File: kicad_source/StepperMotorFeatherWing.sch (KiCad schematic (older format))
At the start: 14 parts, among them CN1 ADAFRUIT_FEATHER, P10 CONN_01X04, P7 CONN_01X04, P8 CONN_01X04, P9 CONN_01X04, Y1 oscillator

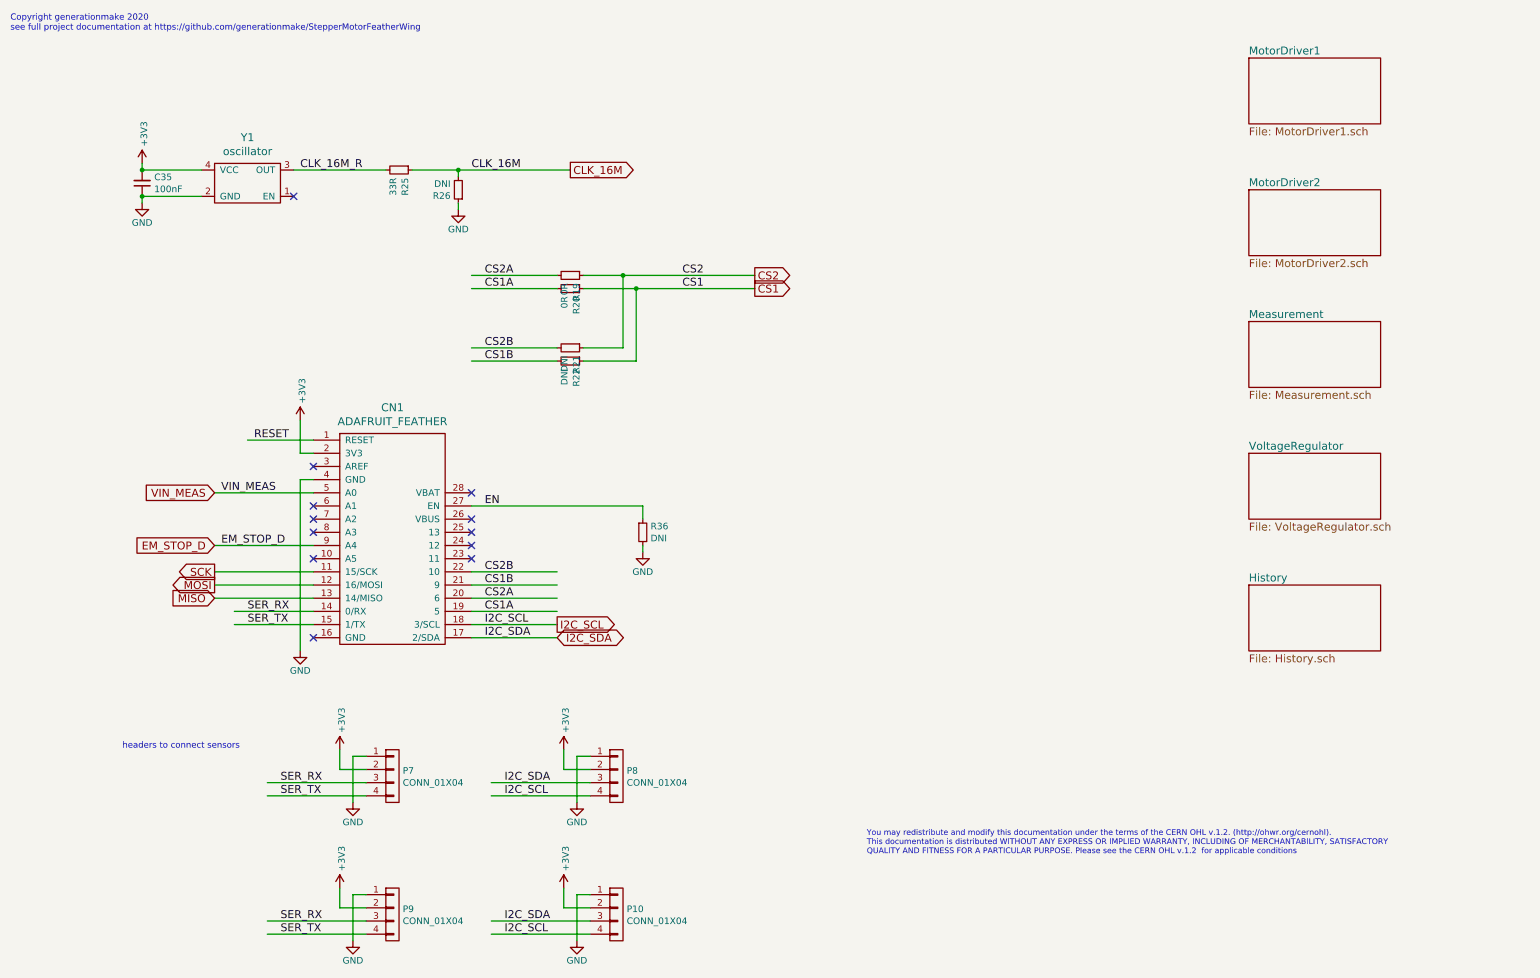
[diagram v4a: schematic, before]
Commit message: added expansion connector, updated layout
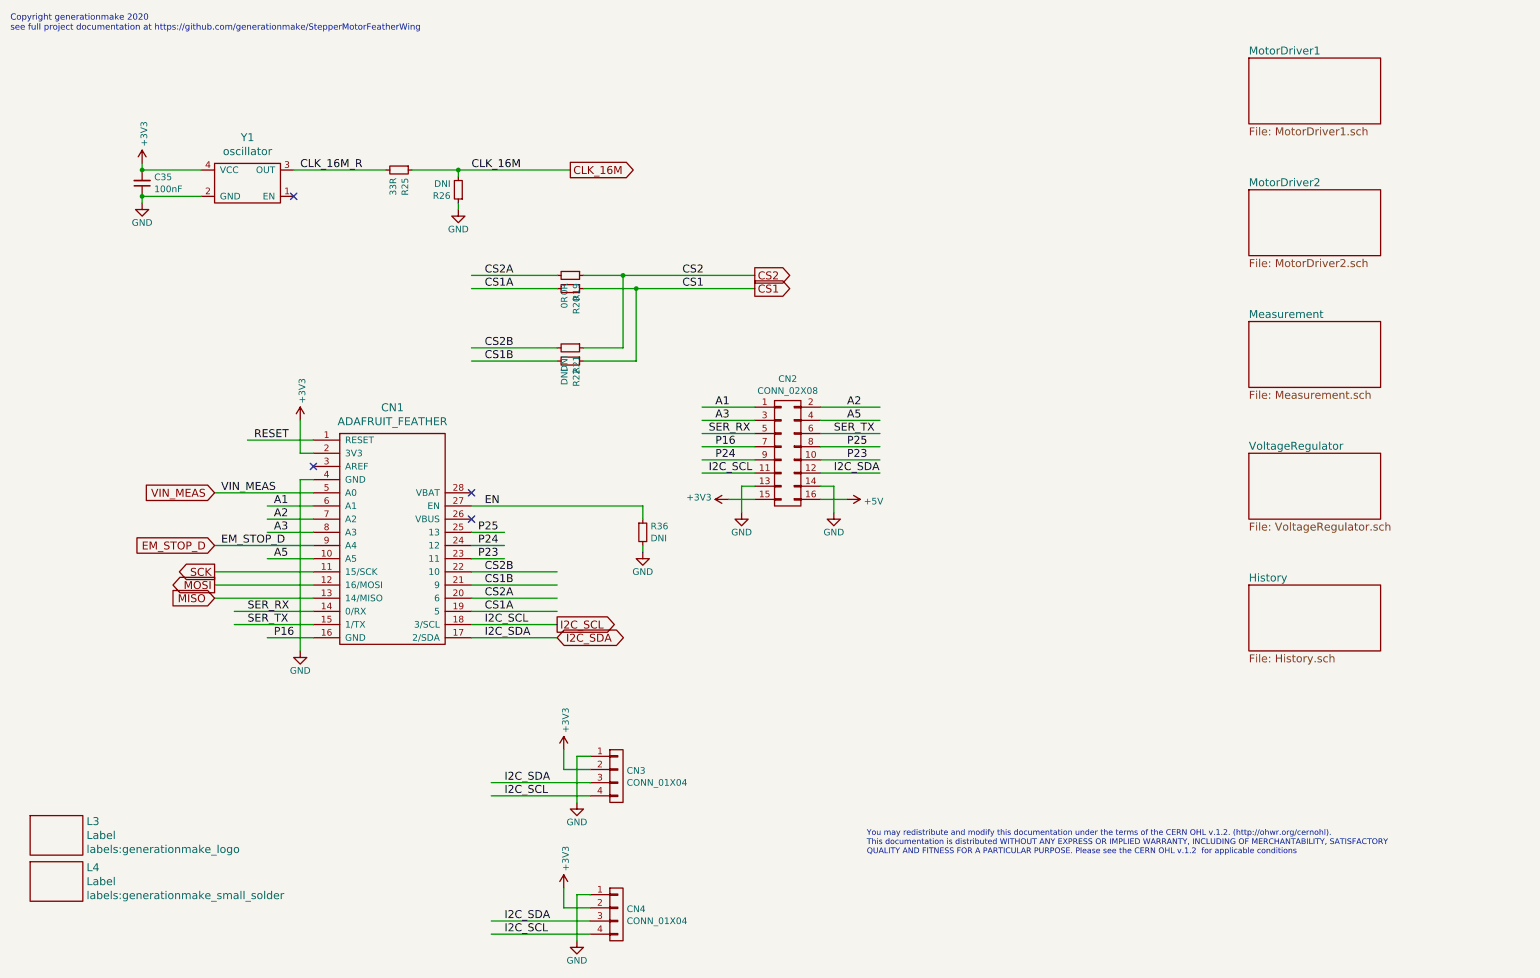
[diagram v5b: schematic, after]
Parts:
- removed P7: CONN_01X04, connectors_JST_SH:Connectors_JST_BM04B-SRSS-TB, symbol mechanical-connectors:CONN_01X04
- removed P9: CONN_01X04, pin_headers:Pin_Header_Straight_1x04, symbol mechanical-connectors:CONN_01X04
- added CN2: CONN_02X08, pin_headers:Pin_Header_Straight_2x08, symbol mechanical-connectors:CONN_02X08
- added L3: Label, labels:generationmake_logo, symbol devices:Label
- added L4: Label, labels:generationmake_small_solder, symbol devices:Label
- renumbered P8 to CN3, P10 to CN4
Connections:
- net labels added: +5V, A1, A2, A3, A5, P16, P23, P24, P25
- wire segments 66 -> 80
- no-connect marks 12 -> 4
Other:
- note removed: "headers to connect sensors"
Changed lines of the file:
@@
 Sheet 1 6
 Title "HighPowerMotorFeatherWing"
-Date "2020-07-04"
+Date "2020-07-08"
 Rev "1.1"
 Comp "generationmake"
@@
 	2050 4150 2800 4150
 NoConn ~ 2800 3950
-NoConn ~ 2800 4250
-NoConn ~ 2800 4350
-NoConn ~ 2800 4450
-NoConn ~ 2800 4650
 NoConn ~ 4000 4350
 NoConn ~ 4000 4150
@@
 Wire Wire Line
 	2700 4050 2700 5350
-NoConn ~ 2800 5250
 $Sheet
 S 9900 3850 1000 500
@@
 Wire Wire Line
 	2050 4550 2800 4550
-NoConn ~ 4000 4450
 $Comp
 L devices:R_0603 R36
@@
 Text GLabel 2050 4950 0    60   Input ~ 0
 MISO
-NoConn ~ 4000 4650
-NoConn ~ 4000 4550
 Text GLabel 6150 2500 2    60   Output ~ 0
 CS2
@@
 CS2
 $Comp
-L mechanical-connectors:CONN_01X04 P8
+L mechanical-connectors:CONN_01X04 CN3
 U 1 1 5DFC9702
 P 5100 6300
-F 0 "P8" H 5178 6341 50  0000 L CNN
+F 0 "CN3" H 5178 6341 50  0000 L CNN
 F 1 "CONN_01X04" H 5178 6250 50  0000 L CNN
 F 2 "connectors_JST_SH:Connectors_JST_BM04B-SRSS-TB" H 5100 6300 50  0001 C CNN
@@
 Text Label 4250 6450 0    60   ~ 0
 I2C_SCL
-$Comp
-L mechanical-connectors:CONN_01X04 P7
-U 1 1 5DFCD1B4
-P 3400 6300
-F 0 "P7" H 3478 6341 50  0000 L CNN
-F 1 "CONN_01X04" H 3478 6250 50  0000 L CNN
-F 2 "connectors_JST_SH:Connectors_JST_BM04B-SRSS-TB" H 3478 6204 50  0001 L CNN
-F 3 "" H 3400 6300 50  0000 C CNN
-	1    3400 6300
-	1    0    0    -1
-$EndComp
-$Comp
-L StepperMotorFeatherWing-rescue:+3V3-power-supply-MKRHMIShield-rescue-MKRHMIShield-rescue-HMIFeatherWing-rescue-HighPowerMotorFeatherWing-rescue #PWR078
-U 1 1 5DFCD1BE
-P 3000 6100
-F 0 "#PWR078" H 3000 5950 50  0001 C CNN
-F 1 "+3V3" V 3015 6228 50  0000 L CNN
-F 2 "" H 3000 6100 50  0000 C CNN
-F 3 "" H 3000 6100 50  0000 C CNN
-	1    3000 6100
-	1    0    0    -1
-$EndComp
-$Comp
-L StepperMotorFeatherWing-rescue:GND-ArduHMIShield-rescue-ArduHMIShield-rescue-MKRHMIShield-rescue-MKRHMIShield-rescue-HMIFeatherWing-rescue-HighPowerMotorFeatherWing-rescue #PWR081
-U 1 1 5DFCD1C8
-P 3100 6500
-F 0 "#PWR081" H 3100 6250 50  0001 C CNN
-F 1 "GND" H 3100 6350 50  0000 C CNN
-F 2 "" H 3100 6500 50  0000 C CNN
-F 3 "" H 3100 6500 50  0000 C CNN
-	1    3100 6500
-	1    0    0    -1
-$EndComp
-Wire Wire Line
-	3200 6150 3100 6150
-Wire Wire Line
-	3100 6150 3100 6500
-Wire Wire Line
-	3200 6250 3000 6250
-Wire Wire Line
-	3000 6250 3000 6100
-Wire Wire Line
-	2450 6350 3200 6350
-Wire Wire Line
-	2450 6450 3200 6450
-Text Label 2550 6350 0    60   ~ 0
-SER_RX
-Text Label 2550 6450 0    60   ~ 0
-SER_TX
 Wire Wire Line
 	2200 5050 2800 5050
@@
 SER_TX
 $Comp
-L mechanical-connectors:CONN_01X04 P10
+L mechanical-connectors:CONN_01X04 CN4
 U 1 1 5DF94AD6
 P 5100 7350
-F 0 "P10" H 5178 7391 50  0000 L CNN
+F 0 "CN4" H 5178 7391 50  0000 L CNN
 F 1 "CONN_01X04" H 5178 7300 50  0000 L CNN
 F 2 "pin_headers:Pin_Header_Straight_1x04" H 5100 7350 50  0001 C CNN
@@
 Text Label 4250 7500 0    60   ~ 0
 I2C_SCL
-$Comp
-L mechanical-connectors:CONN_01X04 P9
-U 1 1 5DF94AFC
-P 3400 7350
-F 0 "P9" H 3478 7391 50  0000 L CNN
-F 1 "CONN_01X04" H 3478 7300 50  0000 L CNN
-F 2 "pin_headers:Pin_Header_Straight_1x04" H 3478 7254 50  0001 L CNN
-F 3 "" H 3400 7350 50  0000 C CNN
-	1    3400 7350
-	1    0    0    -1
-$EndComp
-$Comp
-L StepperMotorFeatherWing-rescue:+3V3-power-supply-MKRHMIShield-rescue-MKRHMIShield-rescue-HMIFeatherWing-rescue-HighPowerMotorFeatherWing-rescue #PWR083
-U 1 1 5DF94B06
-P 3000 7150
-F 0 "#PWR083" H 3000 7000 50  0001 C CNN
-F 1 "+3V3" V 3015 7278 50  0000 L CNN
-F 2 "" H 3000 7150 50  0000 C CNN
-F 3 "" H 3000 7150 50  0000 C CNN
-	1    3000 7150
-	1    0    0    -1
-$EndComp
-$Comp
-L StepperMotorFeatherWing-rescue:GND-ArduHMIShield-rescue-ArduHMIShield-rescue-MKRHMIShield-rescue-MKRHMIShield-rescue-HMIFeatherWing-rescue-HighPowerMotorFeatherWing-rescue #PWR085
-U 1 1 5DF94B10
-P 3100 7550
-F 0 "#PWR085" H 3100 7300 50  0001 C CNN
-F 1 "GND" H 3100 7400 50  0000 C CNN
-F 2 "" H 3100 7550 50  0000 C CNN
-F 3 "" H 3100 7550 50  0000 C CNN
-	1    3100 7550
-	1    0    0    -1
-$EndComp
-Wire Wire Line
-	3200 7200 3100 7200
-Wire Wire Line
-	3100 7200 3100 7550
-Wire Wire Line
-	3200 7300 3000 7300
-Wire Wire Line
-	3000 7300 3000 7150
-Wire Wire Line
-	2450 7400 3200 7400
-Wire Wire Line
-	2450 7500 3200 7500
-Text Label 2550 7400 0    60   ~ 0
-SER_RX
-Text Label 2550 7500 0    60   ~ 0
-SER_TX
-Text Notes 1350 6100 0    47   ~ 0
-headers to connect sensors
 $Comp
 L devices:R_0603 R19
@@
 Text GLabel 4750 1700 2    60   Output ~ 0
 CLK_16M
+$Comp
+L mechanical-connectors:CONN_02X08 CN2
+U 1 1 5F051404
+P 6400 3850
+F 0 "CN2" H 6400 4415 50  0000 C CNN
+F 1 "CONN_02X08" H 6400 4324 50  0000 C CNN
+F 2 "pin_headers:Pin_Header_Straight_2x08" H 6400 2650 50  0001 C CNN
+F 3 "" H 6400 2650 50  0000 C CNN
+	1    6400 3850
+	1    0    0    -1
+$EndComp
+Wire Wire Line
+	2450 4650 2800 4650
+Wire Wire Line
+	2450 4450 2800 4450
+Wire Wire Line
+	2450 4350 2800 4350
+Wire Wire Line
+	2450 4250 2800 4250
+Text Label 2500 4250 0    60   ~ 0
+A1
+Text Label 2500 4350 0    60   ~ 0
+A2
+Text Label 2500 4450 0    60   ~ 0
+A3
+Text Label 2500 4650 0    60   ~ 0
+A5
+Wire Wire Line
+	2450 5250 2800 5250
+Text Label 2500 5250 0    60   ~ 0
+P16
+Wire Wire Line
+	4250 4650 4000 4650
+Wire Wire Line
+	4250 4550 4000 4550
+Wire Wire Line
+	4250 4450 4000 4450
+Text Label 4050 4650 0    60   ~ 0
+P23
+Text Label 4050 4550 0    60   ~ 0
+P24
+Text Label 4050 4450 0    60   ~ 0
+P25
+Wire Wire Line
+	5750 3500 6150 3500
+Wire Wire Line
+	5750 3600 6150 3600
+Wire Wire Line
+	5750 3700 6150 3700
+Wire Wire Line
+	5750 3800 6150 3800
+Wire Wire Line
+	5750 3900 6150 3900
+Wire Wire Line
+	6650 3900 7100 3900
+Wire Wire Line
+	7100 3800 6650 3800
+Wire Wire Line
+	6650 3700 7100 3700
+Wire Wire Line
+	7100 3600 6650 3600
+Wire Wire Line
+	7100 3500 6650 3500
+Text Label 5850 3500 0    60   ~ 0
+A1
+Text Label 6850 3500 0    60   ~ 0
+A2
+Text Label 5850 3600 0    60   ~ 0
+A3
+Text Label 6850 3600 0    60   ~ 0
+A5
+Text Label 5800 3700 0    60   ~ 0
+SER_RX
+Text Label 6750 3700 0    60   ~ 0
+SER_TX
+Text Label 5850 3800 0    60   ~ 0
+P16
+Text Label 6850 3800 0    60   ~ 0
+P25
+Text Label 5850 3900 0    60   ~ 0
+P24
+Text Label 6850 3900 0    60   ~ 0
+P23
+$Comp
+L StepperMotorFeatherWing-rescue:GND-ArduHMIShield-rescue-ArduHMIShield-rescue-MKRHMIShield-rescue-MKRHMIShield-rescue-HMIFeatherWing-rescue-HighPowerMotorFeatherWing-rescue #PWR081
+U 1 1 5F086557
+P 6050 4300
+F 0 "#PWR081" H 6050 4050 50  0001 C CNN
+F 1 "GND" H 6050 4150 50  0000 C CNN
+F 2 "" H 6050 4300 50  0000 C CNN
+F 3 "" H 6050 4300 50  0000 C CNN
+	1    6050 4300
+	1    0    0    -1
+$EndComp
+$Comp
+L StepperMotorFeatherWing-rescue:GND-ArduHMIShield-rescue-ArduHMIShield-rescue-MKRHMIShield-rescue-MKRHMIShield-rescue-HMIFeatherWing-rescue-HighPowerMotorFeatherWing-rescue #PWR083
+U 1 1 5F087252
+P 6750 4300
+F 0 "#PWR083" H 6750 4050 50  0001 C CNN
+F 1 "GND" H 6750 4150 50  0000 C CNN
+F 2 "" H 6750 4300 50  0000 C CNN
+F 3 "" H 6750 4300 50  0000 C CNN
+	1    6750 4300
+	1    0    0    -1
+$EndComp
+$Comp
+L StepperMotorFeatherWing-rescue:+3V3-power-supply-MKRHMIShield-rescue-MKRHMIShield-rescue-HMIFeatherWing-rescue-HighPowerMotorFeatherWing-rescue #PWR078
+U 1 1 5F088175
+P 5950 4200
+F 0 "#PWR078" H 5950 4050 50  0001 C CNN
+F 1 "+3V3" V 5965 4328 50  0000 L CNN
+F 2 "" H 5950 4200 50  0000 C CNN
+F 3 "" H 5950 4200 50  0000 C CNN
+	1    5950 4200
+	0    -1   -1   0
+$EndComp
+$Comp
+L power-supply:+5V #PWR085
+U 1 1 5F088ECF
+P 6850 4200
+F 0 "#PWR085" H 6850 4050 50  0001 C CNN
+F 1 "+5V" V 6865 4328 50  0000 L CNN
+F 2 "" H 6850 4200 50  0000 C CNN
+F 3 "" H 6850 4200 50  0000 C CNN
+	1    6850 4200
+	0    1    1    0
+$EndComp
+Wire Wire Line
+	6050 4300 6050 4100
+Wire Wire Line
+	6750 4300 6750 4100
+Wire Wire Line
+	6850 4200 6650 4200
+Wire Wire Line
+	5950 4200 6150 4200
+Wire Wire Line
+	6150 4100 6050 4100
+Wire Wire Line
+	6650 4100 6750 4100
+Wire Wire Line
+	6650 4000 7100 4000
+Wire Wire Line
+	5750 4000 6150 4000
+Text Label 5800 4000 0    60   ~ 0
+I2C_SCL
+Text Label 6750 4000 0    60   ~ 0
+I2C_SDA
+$Comp
+L devices:Label L3
+U 1 1 5F0B3FD2
+P 850 6750
+F 0 "L3" H 1078 6856 60  0000 L CNN
+F 1 "Label" H 1078 6750 60  0000 L CNN
+F 2 "labels:generationmake_logo" H 1078 6644 60  0000 L CNN
+F 3 "" H 850 6750 60  0000 C CNN
+	1    850  6750
+	1    0    0    -1
+$EndComp
+$Comp
+L devices:Label L4
+U 1 1 5F0B45CF
+P 850 7100
+F 0 "L4" H 1078 7206 60  0000 L CNN
+F 1 "Label" H 1078 7100 60  0000 L CNN
+F 2 "labels:generationmake_small_solder" H 1078 6994 60  0000 L CNN
+F 3 "" H 850 7100 60  0000 C CNN
+	1    850  7100
+	1    0    0    -1
+$EndComp
 $EndSCHEMATC

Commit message: updated part numbers
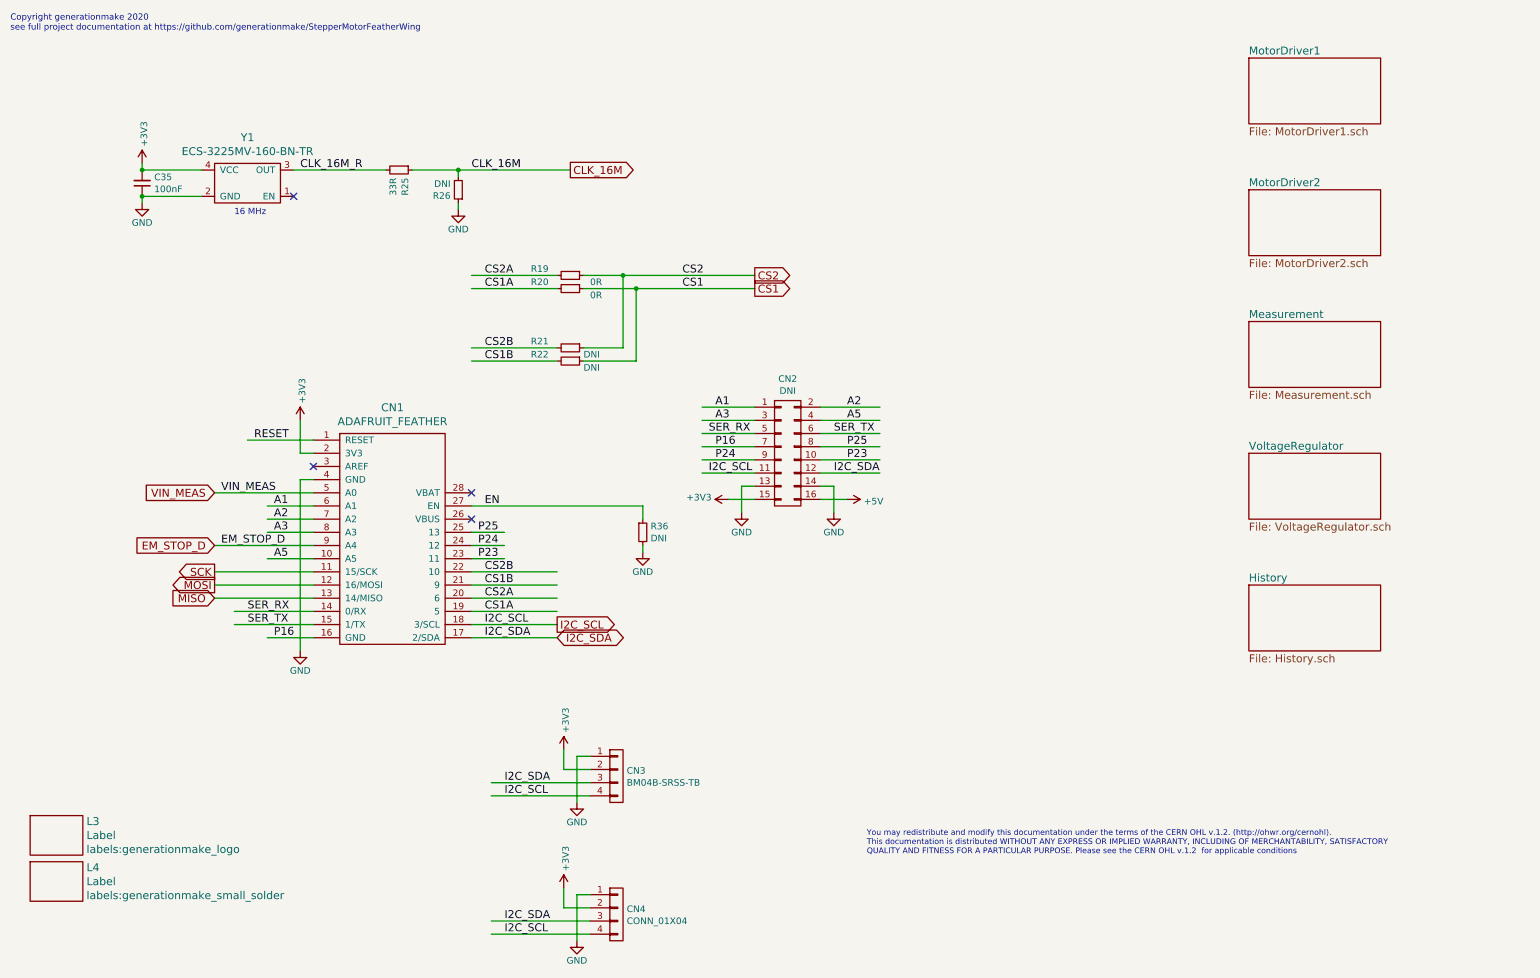
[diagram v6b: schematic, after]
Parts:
- CN2: value CONN_02X08 -> DNI
- CN3: value CONN_01X04 -> BM04B-SRSS-TB
- Y1: value oscillator -> ECS-3225MV-160-BN-TR
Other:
- note added: "16 MHz"
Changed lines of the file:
@@
 P 5100 6300
 F 0 "CN3" H 5178 6341 50  0000 L CNN
-F 1 "CONN_01X04" H 5178 6250 50  0000 L CNN
+F 1 "BM04B-SRSS-TB" H 5178 6250 50  0000 L CNN
 F 2 "connectors_JST_SH:Connectors_JST_BM04B-SRSS-TB" H 5100 6300 50  0001 C CNN
 F 3 "" H 5100 6300 50  0000 C CNN
@@
 U 1 1 5DFA2A5B
 P 4750 2500
-F 0 "R19" H 4809 2546 50  0000 L CNN
-F 1 "0R" H 4809 2455 50  0000 L CNN
+F 0 "R19" V 4700 2200 50  0000 L CNN
+F 1 "0R" V 4800 2650 50  0000 L CNN
 F 2 "resistors:R_0603" H 4750 2350 50  0001 C CNN
 F 3 "" H 4750 2500 50  0000 C CNN
@@
 U 1 1 5DFA3126
 P 4750 2600
-F 0 "R20" H 4809 2646 50  0000 L CNN
-F 1 "0R" H 4809 2555 50  0000 L CNN
+F 0 "R20" V 4700 2300 50  0000 L CNN
+F 1 "0R" V 4800 2750 50  0000 L CNN
 F 2 "resistors:R_0603" H 4750 2450 50  0001 C CNN
 F 3 "" H 4750 2600 50  0000 C CNN
@@
 U 1 1 5DFA32A2
 P 4750 3050
-F 0 "R21" H 4809 3096 50  0000 L CNN
-F 1 "DNI" H 4809 3005 50  0000 L CNN
+F 0 "R21" V 4700 2750 50  0000 L CNN
+F 1 "DNI" V 4800 3150 50  0000 L CNN
 F 2 "resistors:R_0603" H 4750 2900 50  0001 C CNN
 F 3 "" H 4750 3050 50  0000 C CNN
@@
 U 1 1 5DFA3550
 P 4750 3150
-F 0 "R22" H 4809 3196 50  0000 L CNN
-F 1 "DNI" H 4809 3105 50  0000 L CNN
+F 0 "R22" V 4700 2850 50  0000 L CNN
+F 1 "DNI" V 4800 3250 50  0000 L CNN
 F 2 "resistors:R_0603" H 4750 3000 50  0001 C CNN
 F 3 "" H 4750 3150 50  0000 C CNN
@@
 P 2300 1800
 F 0 "Y1" H 2300 2147 60  0000 C CNN
-F 1 "oscillator" H 2300 2041 60  0000 C CNN
+F 1 " ECS-3225MV-160-BN-TR" H 2300 2041 60  0000 C CNN
 F 2 "crystals:Crystal_SMD_3.2x2.5mm_4Pad" H 2300 1800 60  0001 C CNN
 F 3 "" H 2300 1800 60  0001 C CNN
@@
 P 6400 3850
 F 0 "CN2" H 6400 4415 50  0000 C CNN
-F 1 "CONN_02X08" H 6400 4324 50  0000 C CNN
+F 1 "DNI" H 6400 4324 50  0000 C CNN
 F 2 "pin_headers:Pin_Header_Straight_2x08" H 6400 2650 50  0001 C CNN
 F 3 "" H 6400 2650 50  0000 C CNN
@@
 	1    0    0    -1
 $EndComp
+Text Notes 2200 2050 0    47   ~ 0
+16 MHz
 $EndSCHEMATC
